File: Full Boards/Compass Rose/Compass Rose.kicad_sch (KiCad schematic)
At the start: 248 parts, among them J1 Program Header, J3 Optional Bond, Q1 BSS314PE, Q2 DMN6075S, Q3 BSS314PE, Q4 DMN6075S, Q5 BSS314PE, Q6 DMN6075S, SW1 Boot, SW2 Reset, SW3 CTS_219-2MSTR

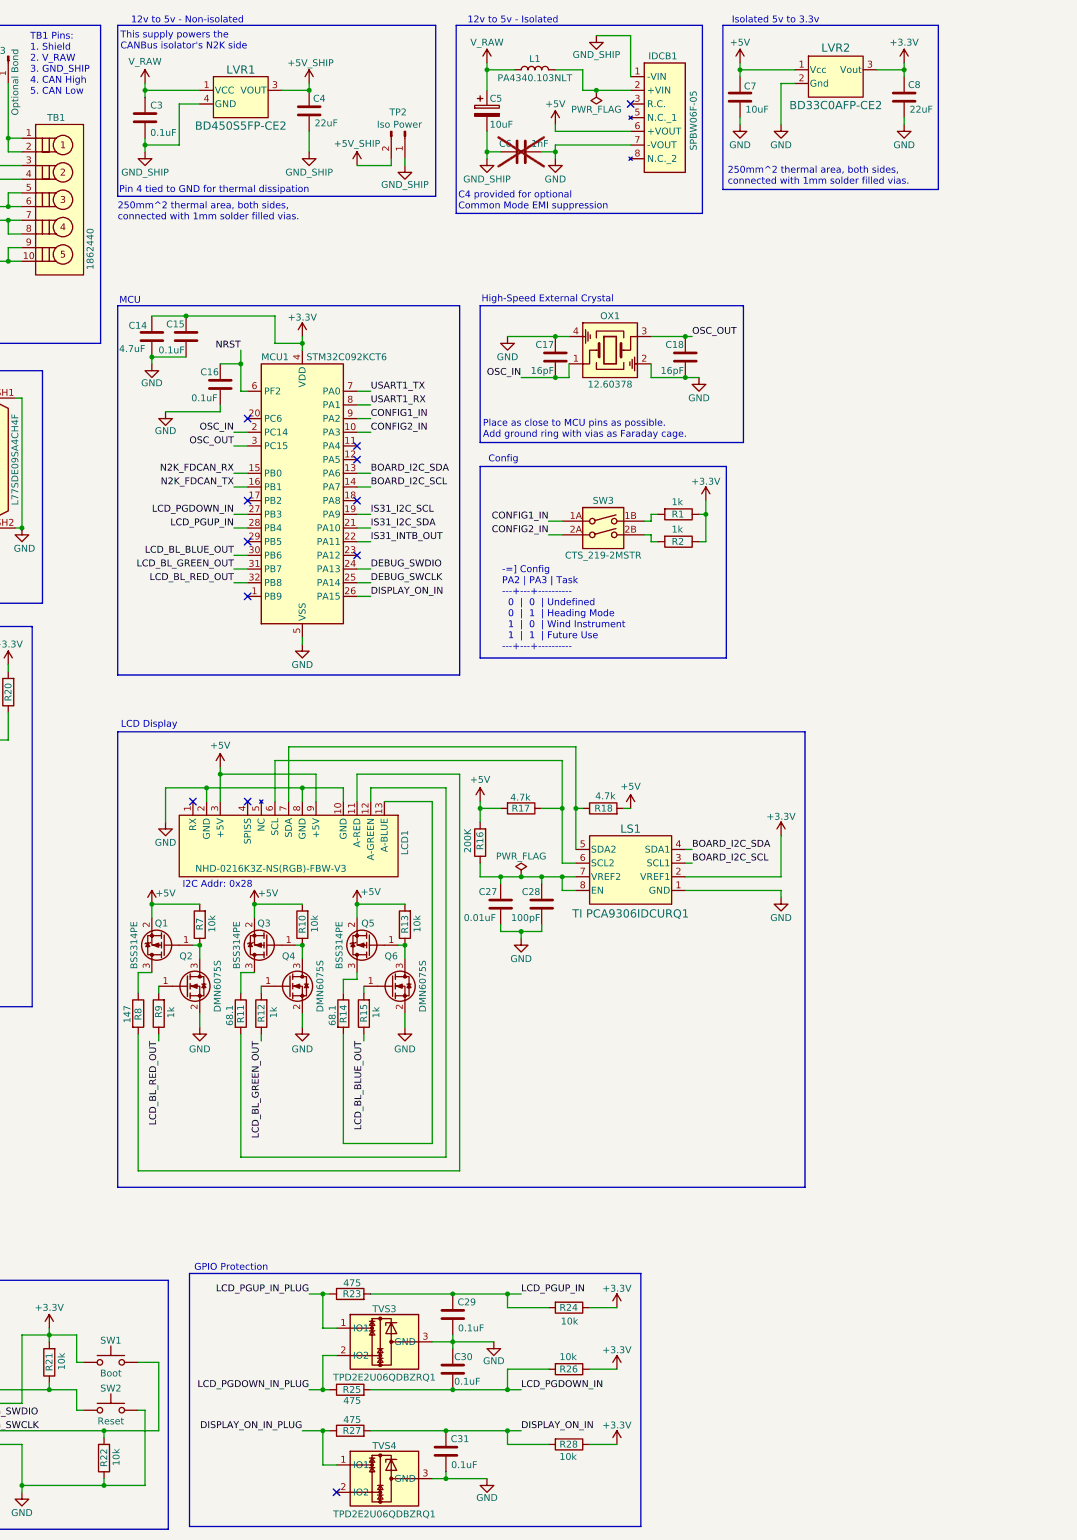
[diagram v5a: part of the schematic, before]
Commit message: Routed missed resistors.
Signed-off-by: digimer <digital.mermaid@gmail.com>
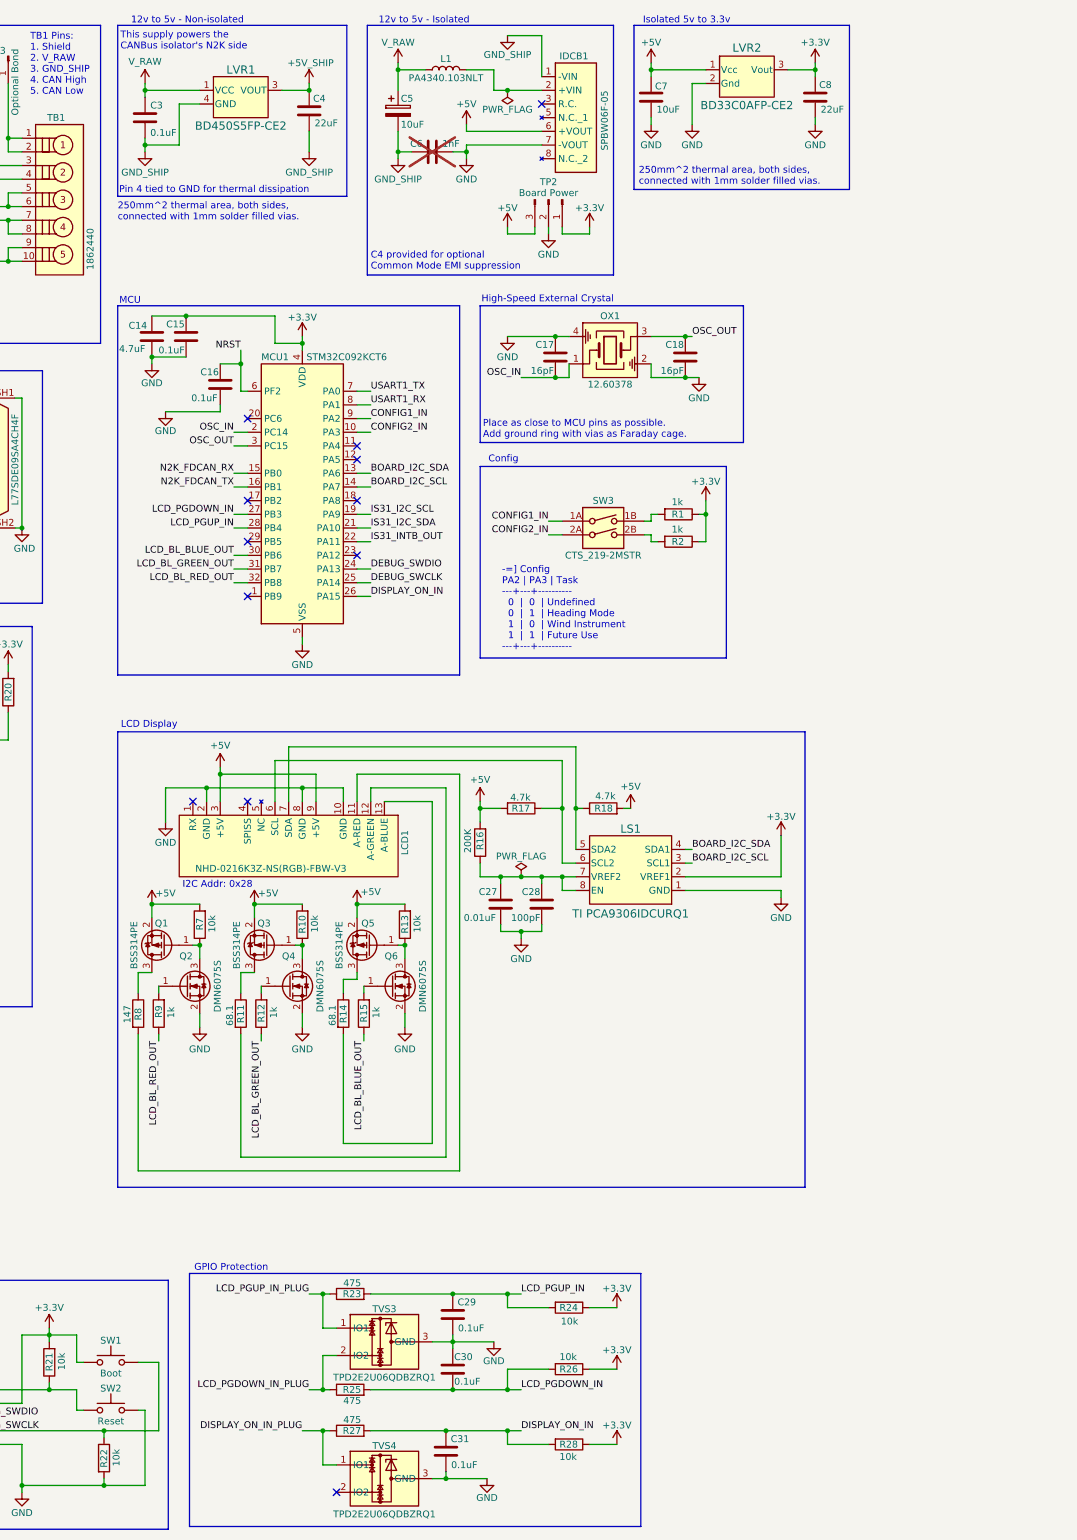
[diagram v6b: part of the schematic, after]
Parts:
- TP2: value Iso Power -> Board Power; footprint Connector_PinHeader_2.54mm:PinHeader_1x02_P2.54mm_Vertical -> Connector_PinHeader_2.54mm:PinHeader_1x03_P2.54mm_Vertical; symbol Connector:Conn_01x02_Pin -> Connector:Conn_01x03_Pin
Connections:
- net +3.3V: now also TP2.1 (Pin_1)
- net +5V: now also TP2.3 (Pin_3)
- net +5V_SHIP: no longer TP2.2 (Pin_2)
- net DEBUG_SWCLK: now also R22.1; no longer R22.2
- net GND: now also R22.2, TP2.2 (Pin_2); no longer R22.1
- net GND_SHIP: no longer TP2.1 (Pin_1)
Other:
- moved on the sheet: C5, C6, C7, C8, IDCB1, L1, LVR2, R22

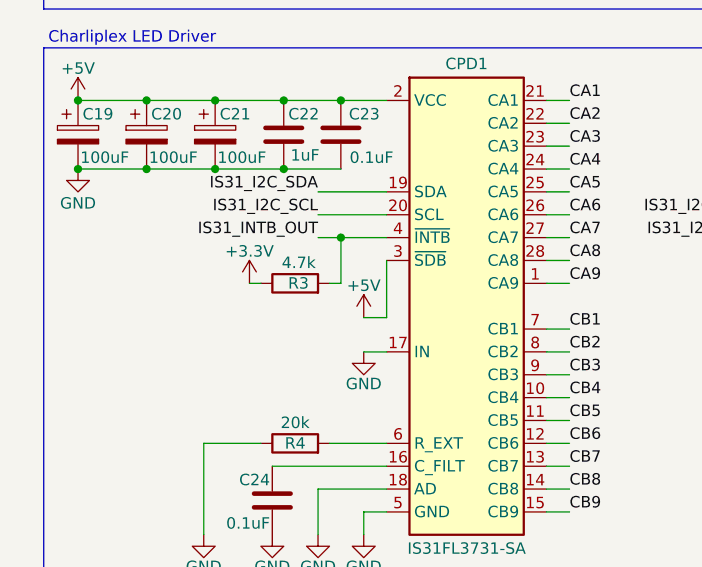
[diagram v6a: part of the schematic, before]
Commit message: DRC is clear, fixed some footprints.
Signed-off-by: digimer <digital.mermaid@gmail.com>
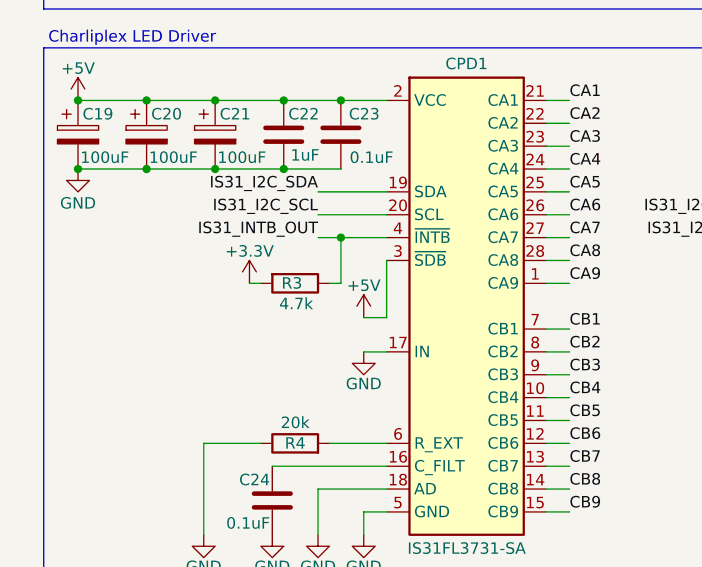
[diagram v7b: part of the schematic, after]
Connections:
- net +3.3V: now also R3.2; no longer R3.1
- net IS31_INTB_OUT: now also R3.1; no longer R3.2
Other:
- moved on the sheet: R3
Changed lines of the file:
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@@
 	(symbol
 		(lib_id "Device:R")
-		(at 43.18 153.67 90)
+		(at 43.18 153.67 270)
 		(unit 1)
 		(body_style 1)
@@
 		(dnp no)
 		(property "Reference" "R3"
-			(at 44.704 153.67 90)
+			(at 41.656 153.67 90)
 			(show_name no)
 			(do_not_autoplace no)
@@
 		)
 		(property "Value" "4.7k"
-			(at 45.466 151.384 90)
+			(at 41.402 155.956 90)
 			(show_name no)
 			(do_not_autoplace no)
@@
 		)
 		(property "Footprint" "mr-stuff:Stackpole RMCA0805"
-			(at 43.18 155.448 90)
+			(at 43.18 151.892 90)
 			(hide yes)
 			(show_name no)
